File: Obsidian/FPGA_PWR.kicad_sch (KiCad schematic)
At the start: 52 parts, among them U1 XC7A35T-CSG325

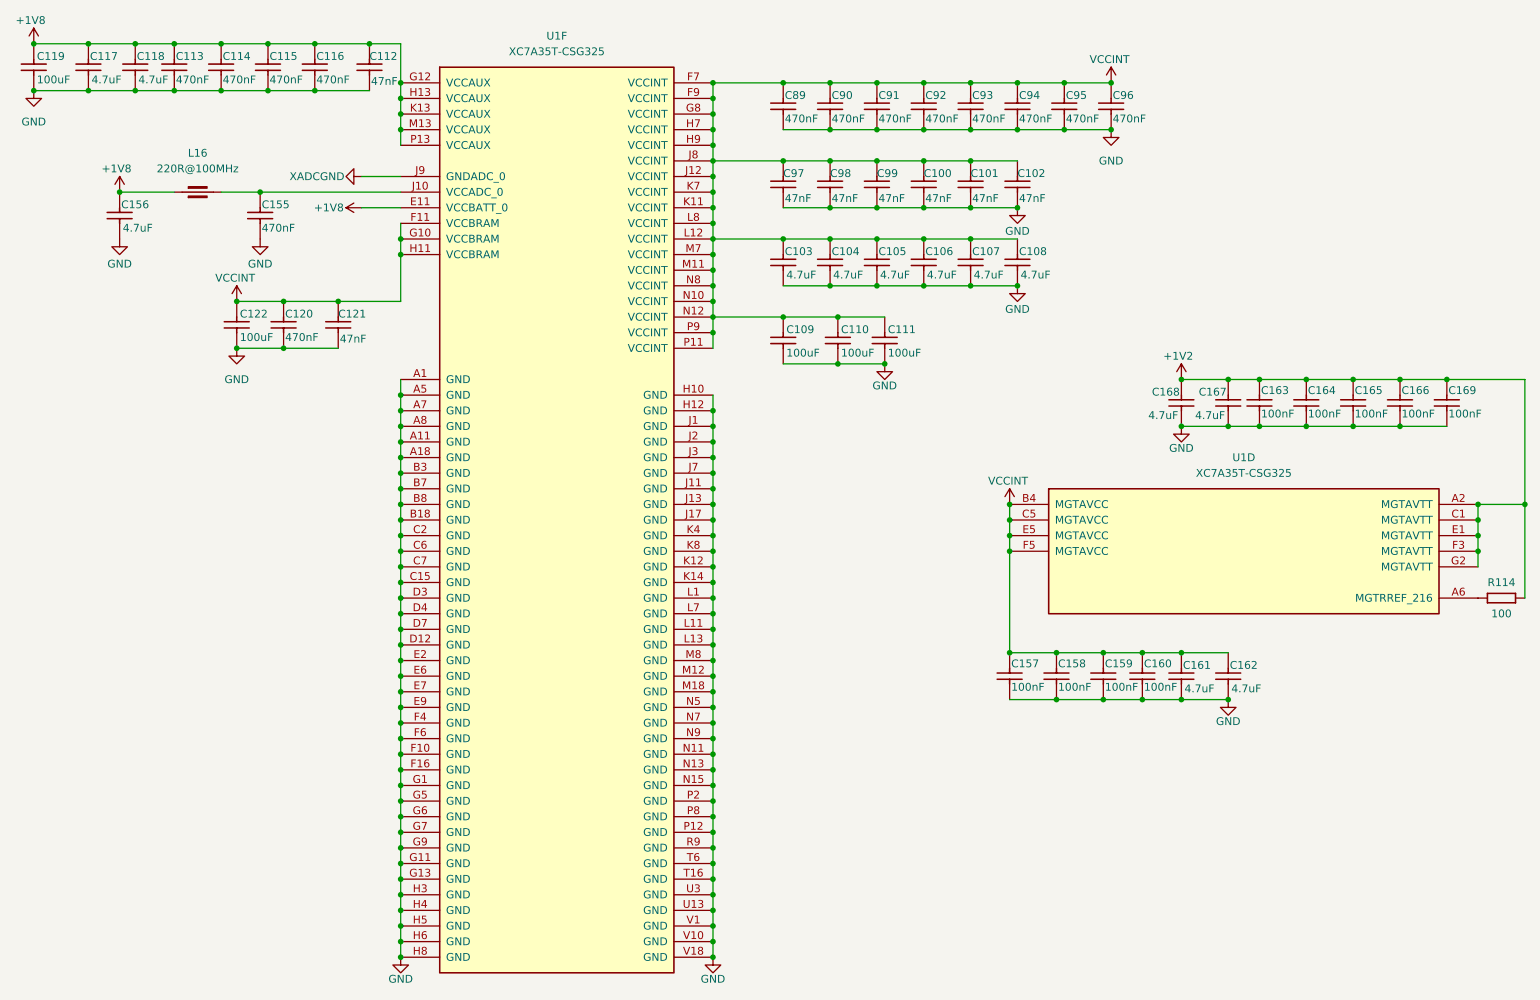
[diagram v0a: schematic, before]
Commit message: Removing unnecessary components for the interface. Adding SPIN schematic and footprint
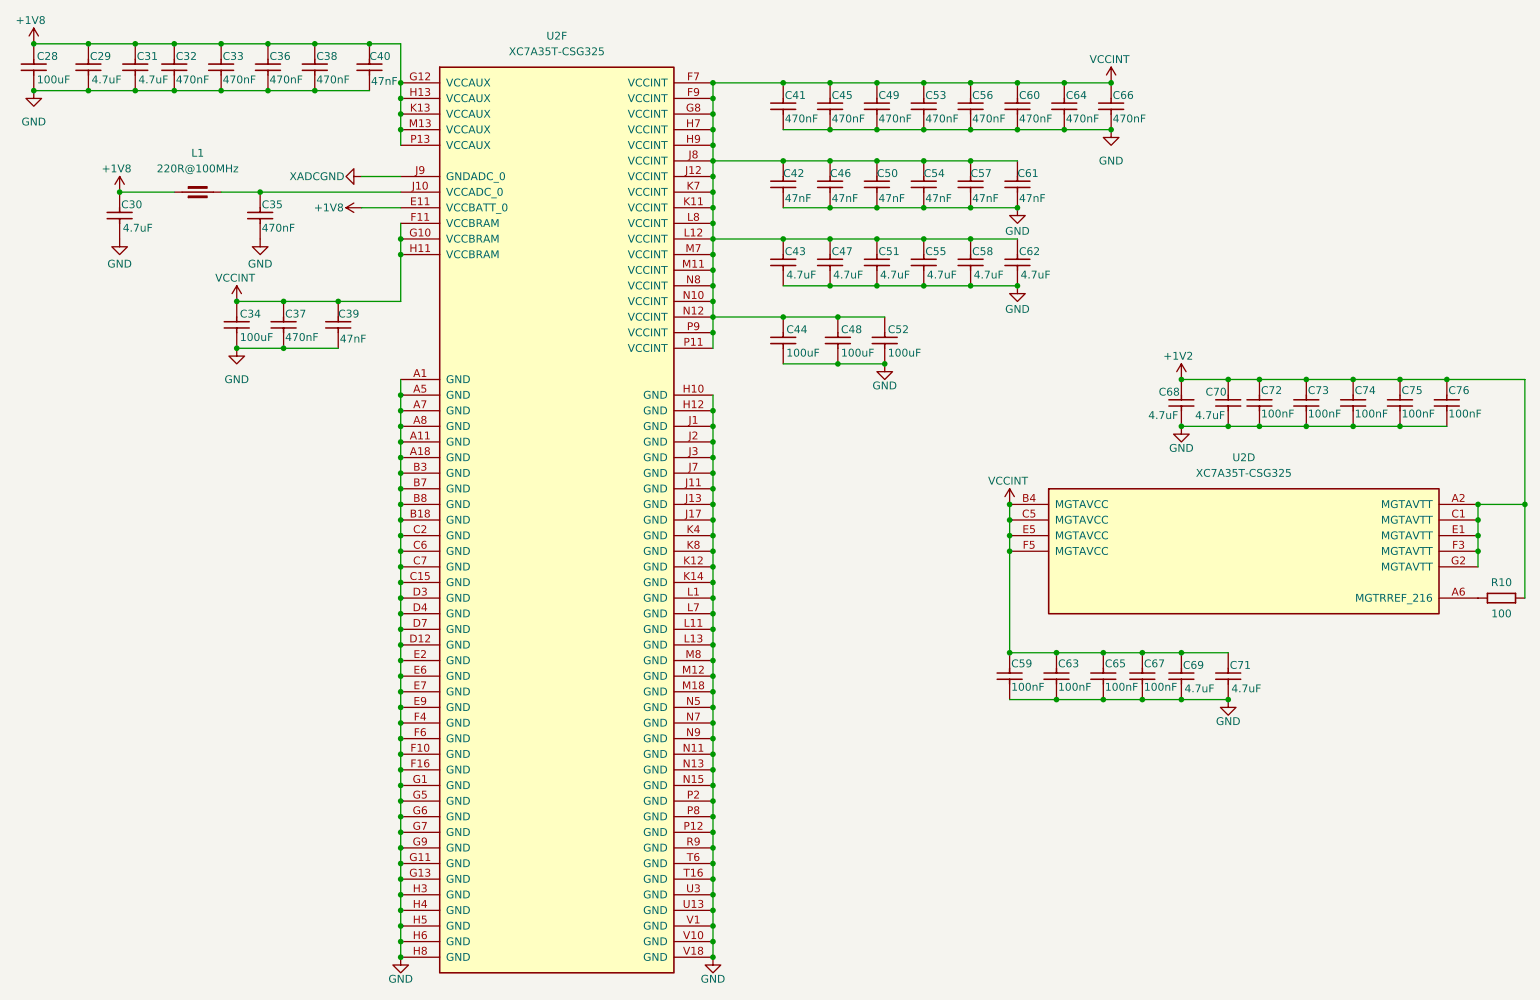
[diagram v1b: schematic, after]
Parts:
- renumbered C119 to C28, C117 to C29, C156 to C30, C118 to C31, C113 to C32, C114 to C33, C122 to C34, C155 to C35, C115 to C36, C120 to C37, C116 to C38, C121 to C39, C112 to C40, C89 to C41, C97 to C42, C103 to C43, C109 to C44, C90 to C45, C98 to C46, C104 to C47, C110 to C48, C91 to C49, C99 to C50, C105 to C51, C111 to C52, C92 to C53, C100 to C54, C106 to C55, C93 to C56, C101 to C57, C107 to C58, C157 to C59, C94 to C60, C102 to C61, C108 to C62, C158 to C63, C95 to C64, C159 to C65, C96 to C66, C160 to C67, C168 to C68, C161 to C69, C167 to C70, C162 to C71, C163 to C72, C164 to C73, C165 to C74, C166 to C75, C169 to C76, L16 to L1, R114 to R10, U1 to U2
